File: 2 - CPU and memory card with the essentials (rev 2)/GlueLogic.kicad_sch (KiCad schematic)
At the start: 15 parts, among them U2 ATF22V10C, U3 ATF16V8B, U4 ATF22V10C, U5 ATF22V10C

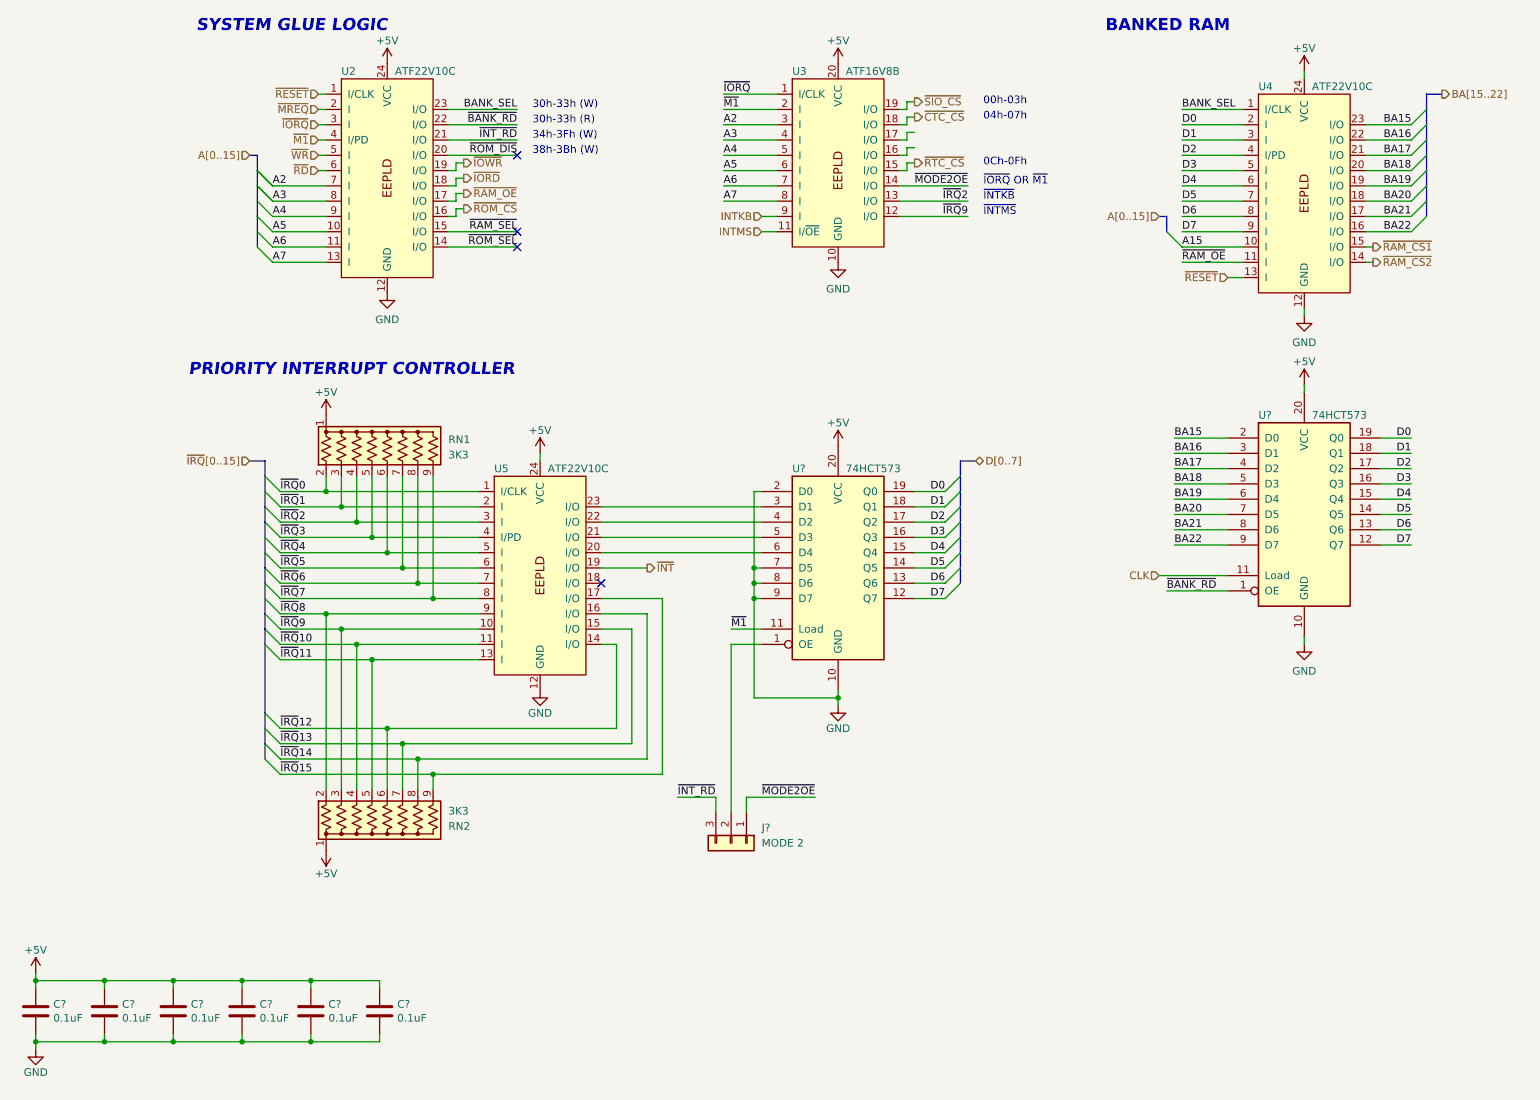
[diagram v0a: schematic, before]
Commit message: Updated disk activity circuit in mother board, and improved layout in CPU card
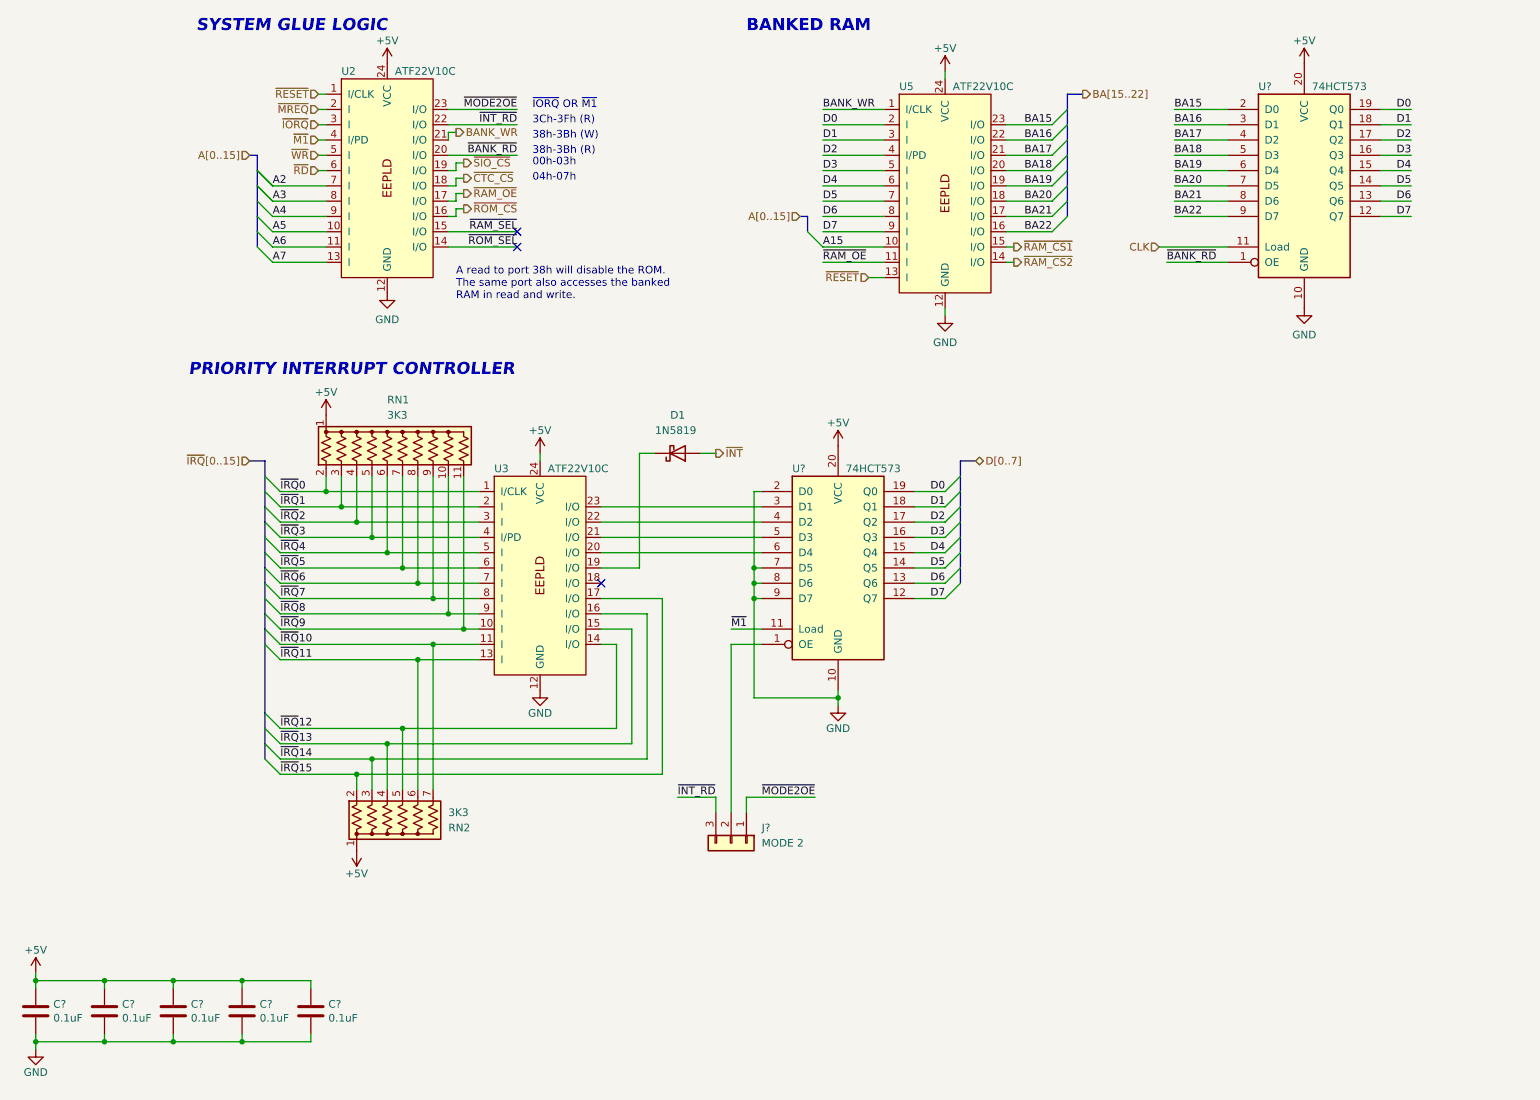
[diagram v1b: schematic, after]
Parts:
- removed C?: 0.1uF, Capacitor_THT:C_Disc_D3.0mm_W2.0mm_P2.50mm, symbol Device:C
- removed U3: ATF16V8B, Package_DIP:DIP-20_W7.62mm_LongPads, symbol 0_Library:ATF16V8B
- added D1: 1N5819, Diode_THT:D_DO-41_SOD81_P10.16mm_Horizontal, symbol Diode:1N5819
- RN1: footprint Resistor_THT:R_Array_SIP9 -> Resistor_THT:R_Array_SIP11; symbol Device:R_Network08_US -> Device:R_Network10_US
- RN2: footprint Resistor_THT:R_Array_SIP9 -> Resistor_THT:R_Array_SIP7; symbol Device:R_Network08_US -> Device:R_Network06_US
- renumbered U5 to U3, U4 to U5
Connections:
- net ~{IORD} is gone; now on net ~{CTC_CS}: U2.18 (I/O)
- net ~{IOWR} is gone; now on net ~{SIO_CS}: U2.19 (I/O)
- net ~{ROM_DIS} is gone; now on net ~{BANK_RD}: U2.20 (I/O)
- net ~{BANK_RD}: no longer U2.22 (I/O)
- net ~{INT_RD}: now also U2.22 (I/O); no longer U2.21 (I/O)
- net ~{INT}: now also D1.2 (A); no longer U3.19 (I/O)
- net ~{IRQ}10: now also RN2.7 (R6); no longer RN2.4 (R3)
- net ~{IRQ}11: now also RN2.6 (R5); no longer RN2.5 (R4)
- net ~{IRQ}12: now also RN2.5 (R4); no longer RN2.6 (R5)
- net ~{IRQ}13: now also RN2.4 (R3); no longer RN2.7 (R6)
- net ~{IRQ}14: now also RN2.3 (R2); no longer RN2.8 (R7)
- net ~{IRQ}15: now also RN2.2 (R1); no longer RN2.9 (R8)
- net ~{IRQ}8: now also RN1.10 (R9); no longer RN2.2 (R1)
- net ~{IRQ}9: now also RN1.11 (R10); no longer RN2.3 (R2)
- net ~{MODE2OE}: now also U2.23 (I/O)
- net BANK_SEL renamed BANK_WR
- net BANK_WR: now also U2.21 (I/O); no longer U2.23 (I/O)
- new net: D1.1 (K), U3.19 (I/O)
- no-connect marks 4 -> 3
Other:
- note added: "38h-3Bh (R)"
- note added: "3Ch-3Fh (R)"
- note added: "A read to port 38h will disable the ROM. The same port also accesses the banked RAM in read and write."
- note removed: "0Ch-0Fh"
- note removed: "30h-33h (R)"
- note removed: "30h-33h (W)"
- note removed: "34h-3Fh (W)"
- note removed: "~{INTKB}"
- note removed: "~{INTMS}"
- moved on the sheet: U5, U?

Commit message: Trying to hash out the flaws
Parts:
- removed D1: 1N5819, Diode_THT:D_DO-41_SOD81_P10.16mm_Horizontal, symbol Diode:1N5819
- removed J?: MODE 2, Connector_PinHeader_2.54mm:PinHeader_1x03_P2.54mm_Vertical, symbol Connector_Generic:Conn_01x03
- removed RN1: 3K3, Resistor_THT:R_Array_SIP11, symbol Device:R_Network10_US
- removed RN2: 3K3, Resistor_THT:R_Array_SIP7, symbol Device:R_Network06_US
- removed U2, U3, U5: ATF22V10C, Package_DIP:DIP-24_W7.62mm_Socket, symbol 0_Library:ATF22V10C
- removed U? (x2): 74HCT573, Package_DIP:DIP-20_W7.62mm_Socket, symbol 74xx:74LS573
- added C? (x2): 0.1uF, Capacitor_THT:C_Disc_D3.0mm_W2.0mm_P2.50mm, symbol Device:C
- added RN4: 3K3, Resistor_THT:R_Array_SIP9, symbol Device:R_Network08_US
- added U10: 74HCT148, symbol 74xx:74LS148
- added U14: 74HCT573, symbol 74xx:74LS573
- added U15: 74HCT138, symbol 74xx:74LS138
- added U2: 74LS574, symbol 74xx:74LS574
- added U3, U6: 74HCT32, symbol 74xx:74LS32
- added U4: 74HCT132, symbol 74xx:74LS132
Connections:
- net +5V: now also C?.1, C?.1, RN4.1 (common), U10.16 (VCC), U14.20 (VCC), U15.16 (VCC), U2.20 (VCC), U3.14 (VCC), U4.14 (VCC), U6.14 (VCC)
- net A15: now also U6.1, U6.12, U6.4, U6.9
- net A3: now also U15.1 (A0)
- net A4: now also U15.2 (A1)
- net A5: now also U15.3 (A2)
- net A6: now also U3.12
- net A7: now also U3.13
- net BA15: now also U6.3
- net BA16: now also U6.6
- net BA17: now also U6.8
- net BA18: now also U6.11
- net D0: now also U14.19 (Q0), U2.2 (D0)
- net D1: now also U14.18 (Q1), U2.3 (D1)
- net D2: now also U14.17 (Q2), U2.4 (D2)
- net D3: now also U14.16 (Q3), U2.5 (D3)
- net D4: now also U14.15 (Q4)
- net D5: now also U14.14 (Q5)
- net D6: now also U14.13 (Q6)
- net D7: now also U14.12 (Q7)
- net GND: now also C?.2, C?.2, U10.5 (EI), U10.8 (GND), U15.8 (GND), U2.1 (OE), U3.7 (GND), U4.7 (GND), U6.7 (GND)
- net ~{CTC_CS}: now also U15.14 (O1)
- net ~{INT}: now also U10.14 (GS)
- net ~{IORQ}: now also U15.5 (E2), U3.10
- net ~{IRQ}0: now also RN4.7 (R6), U10.4 (I7)
- net ~{IRQ}1: now also RN4.5 (R4), U10.3 (I6)
- net ~{IRQ}2: now also RN4.3 (R2), U10.2 (I5)
- net ~{IRQ}3: now also RN4.2 (R1), U10.1 (I4)
- net ~{IRQ}4: now also RN4.4 (R3), U10.13 (I3)
- net ~{IRQ}5: now also RN4.6 (R5), U10.12 (I2)
- net ~{IRQ}6: now also RN4.8 (R7), U10.11 (I1)
- net ~{IRQ}7: now also RN4.9 (R8), U10.10 (IO)
- net ~{M1}: now also U14.11 (Load), U15.6 (E3), U3.9
- net ~{MREQ}: now also U3.4
- net ~{RAM_OE}: now also U3.3
- net ~{RD}: now also U3.2
- net ~{RESET}: now also U4.1
- net ~{ROM_CS}: now also U3.6
- net ~{SIO_CS}: now also U15.15 (O0)
- new net: U3.1, U4.3, U4.4
- new net: U3.5, U4.2, U4.6
- new net: U10.6 (S2), U14.5 (D3)
- new net: U10.7 (S1), U14.4 (D2)
- new net: U10.9 (S0), U14.3 (D1)
- new net: U2.17 (Q2), U6.10
- new net: U2.16 (Q3), U6.13
- new net: U2.18 (Q1), U6.5
- new net: U2.19 (Q0), U6.2
- new net: U15.4 (E1), U3.11
- new net: U14.1 (OE), U3.8
- new net: U14.10 (GND), U14.2 (D0), U14.6 (D4), U14.7 (D5), U14.8 (D6), U14.9 (D7)
- new net ~{BANK_SEL}: U15.9 (O6), U2.11 (Cp)
- new net ~{CF_CS}: U15.13 (O2)
- new net ~{ROM_DIS}: U15.7 (O7), U4.5
- no-connect marks 3 -> 6
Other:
- note added: "00h-07h"
- note added: "08h-0Fh"
- note added: "10h-17h"
- note added: "30h-37h"
- note added: "38h-3Fh"
- note added: "SHADOW LOGIC"
- note removed: "00h-03h"
- note removed: "04h-07h"
- note removed: "38h-3Bh (R)"
- note removed: "38h-3Bh (W)"
- note removed: "3Ch-3Fh (R)"
- note removed: "A read to port 38h will disable the ROM. The same port also accesses the banked RAM in read and write."
- note removed: "~{IORQ} OR ~{M1}"
- moved on the sheet: C?
